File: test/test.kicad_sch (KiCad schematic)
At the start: 3 parts, among them U1 CHIP-PRO

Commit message: big update
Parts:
- LedRef: renamed from D1; value LED -> 100V; footprint LED_SMD:LED_01005_0402Metric -> (none)
- U1: value CHIP-PRO -> CHIP; now not fitted; now left out of the parts list
- renumbered R1 to REFR
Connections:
- net at U1.18 (HPL): now also U1.22 (PB6/I2S-BCLK), U1.23 (PB7/I2S-LCLK), U1.24 (PB8/I2S-DO), U1.25 (PB9/I2S-DI); no longer REFR.2
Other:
- company: SELAB INC -> (none)
- moved on the sheet: REFR
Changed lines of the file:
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@@
 		(title "BestBoard")
 		(date "2026-07-03")
-		(rev "v1")
-		(company "SELAB INC")
 		(comment 1 "c1")
+		(comment 2 "dsaf")
 	)
 	(junction
@@
 		(color 0 0 0 0)
 	)
+	(junction
+		(at 171.45 100.33)
+		(diameter 0)
+		(color 0 0 0 0)
+	)
+	(junction
+		(at 171.45 102.87)
+		(diameter 0)
+		(color 0 0 0 0)
+	)
+	(junction
+		(at 171.45 97.79)
+		(diameter 0)
+		(color 0 0 0 0)
+	)
+	(junction
+		(at 171.45 95.25)
+		(diameter 0)
+		(color 0 0 0 0)
+	)
 	(wire
 		(pts
@@
 	(wire
 		(pts
+			(xy 171.45 102.87) (xy 171.45 107.95)
+		)
+		(stroke
+			(width 0)
+			(type default)
+		)
+	)
+	(wire
+		(pts
+			(xy 171.45 100.33) (xy 171.45 102.87)
+		)
+		(stroke
+			(width 0)
+			(type default)
+		)
+	)
+	(wire
+		(pts
 			(xy 161.29 130.81) (xy 171.45 130.81)
 		)
@@
 	(wire
 		(pts
-			(xy 171.45 106.68) (xy 171.45 107.95)
+			(xy 171.45 93.98) (xy 171.45 95.25)
+		)
+		(stroke
+			(width 0)
+			(type default)
+		)
+	)
+	(wire
+		(pts
+			(xy 171.45 95.25) (xy 171.45 97.79)
 		)
 		(stroke
@@
 	(wire
 		(pts
-			(xy 76.2 106.68) (xy 171.45 106.68)
+			(xy 171.45 97.79) (xy 171.45 100.33)
+		)
+		(stroke
+			(width 0)
+			(type default)
+		)
+	)
+	(wire
+		(pts
+			(xy 24.13 93.98) (xy 171.45 93.98)
 		)
 		(stroke
@@
 		(body_style 1)
 		(exclude_from_sim no)
-		(in_bom yes)
-		(on_board yes)
+		(in_bom no)
+		(on_board no)
 		(in_pos_files yes)
-		(dnp no)
+		(dnp yes)
 		(fields_autoplaced yes)
 		(property "Reference" "U1"
@@
 			)
 		)
-		(property "Value" "CHIP-PRO"
+		(property "Value" "CHIP"
 			(at 214.2333 57.15 0)
 			(show_name no)
@@
 		(dnp no)
 		(fields_autoplaced yes)
-		(property "Reference" "D1"
+		(property "Reference" "LedRef"
 			(at 129.2225 59.69 0)
 			(show_name no)
@@
 			)
 		)
-		(property "Value" "LED"
+		(property "Value" "100V"
 			(at 129.2225 62.23 0)
 			(show_name no)
@@
 			)
 		)
-		(property "Footprint" "LED_SMD:LED_01005_0402Metric"
+		(property "Footprint" ""
 			(at 130.81 66.04 0)
 			(hide yes)
@@
 			(project "test"
 				(path "/2fe60de8-5e34-47a1-855a-3a2b581508e8"
-					(reference "D1")
+					(reference "LedRef")
 					(unit 1)
 				)
@@
 	(symbol
 		(lib_id "Device:R")
-		(at 76.2 102.87 0)
+		(at 24.13 90.17 270)
 		(unit 1)
 		(body_style 1)
@@
 		(dnp no)
 		(fields_autoplaced yes)
-		(property "Reference" "R1"
-			(at 78.74 101.5999 0)
-			(show_name no)
-			(do_not_autoplace no)
-			(effects
-				(font
-					(size 1.27 1.27)
-				)
-				(justify left)
+		(property "Reference" "REFR"
+			(at 24.13 83.82 90)
+			(show_name no)
+			(do_not_autoplace no)
+			(effects
+				(font
+					(size 1.27 1.27)
+				)
 			)
 		)
 		(property "Value" "R"
-			(at 78.74 104.1399 0)
-			(show_name no)
-			(do_not_autoplace no)
-			(effects
-				(font
-					(size 1.27 1.27)
-				)
-				(justify left)
+			(at 24.13 86.36 90)
+			(show_name no)
+			(do_not_autoplace no)
+			(effects
+				(font
+					(size 1.27 1.27)
+				)
 			)
 		)
 		(property "Footprint" "Resistor_SMD:R_01005_0402Metric"
-			(at 74.422 102.87 90)
+			(at 24.13 88.392 90)
 			(hide yes)
 			(show_name no)
@@
 		)
 		(property "Datasheet" ""
-			(at 76.2 102.87 0)
+			(at 24.13 90.17 0)
 			(hide yes)
 			(show_name no)
@@
 		)
 		(property "Description" "Resistor"
-			(at 76.2 102.87 0)
+			(at 24.13 90.17 0)
 			(hide yes)
 			(show_name no)
@@
 			(project "test"
 				(path "/2fe60de8-5e34-47a1-855a-3a2b581508e8"
-					(reference "R1")
+					(reference "REFR")
 					(unit 1)
 				)

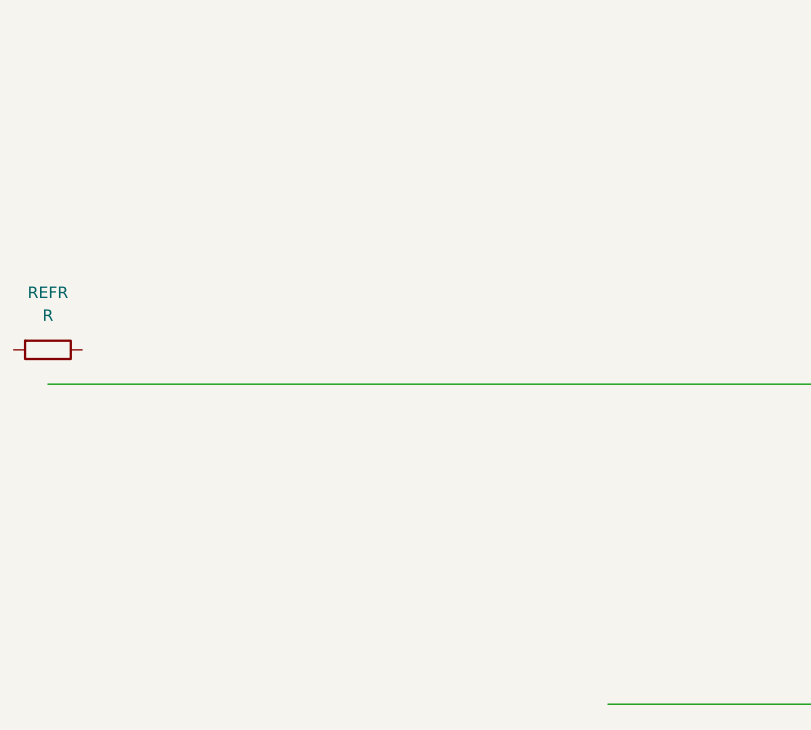
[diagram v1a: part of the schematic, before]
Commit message: added 2 subsheets
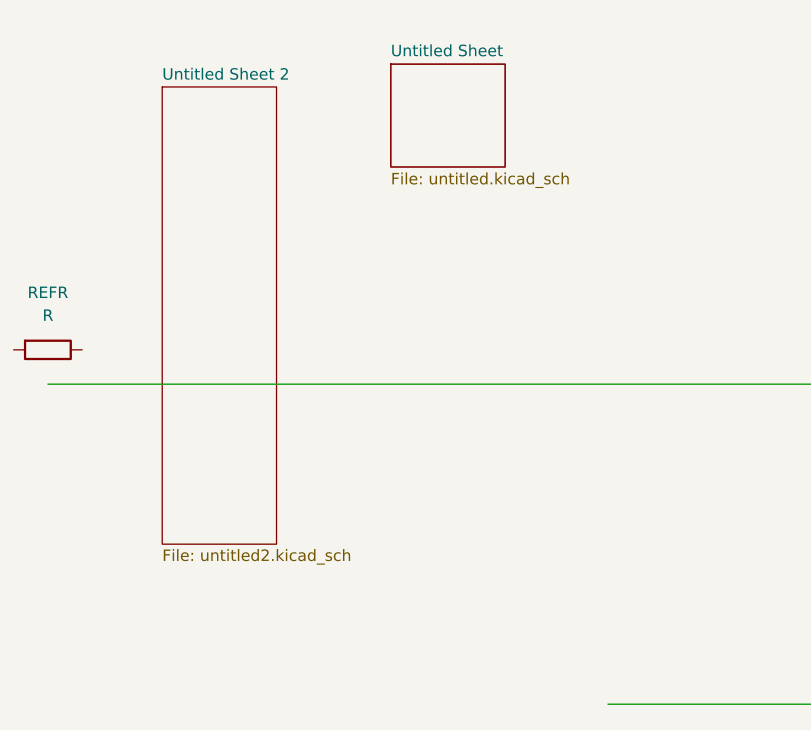
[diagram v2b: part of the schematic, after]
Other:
- added sheet Untitled Sheet (untitled.kicad_sch)
- added sheet Untitled Sheet 2 (untitled2.kicad_sch)
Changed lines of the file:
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@@
+		)
+	)
+	(sheet
+		(at 62.23 58.42)
+		(size 12.7 11.43)
+		(exclude_from_sim no)
+		(in_bom yes)
+		(on_board yes)
+		(dnp no)
+		(fields_autoplaced yes)
+		(stroke
+			(width 0.1778)
+			(type solid)
+		)
+		(fill
+			(color 0 0 0 0)
+		)
+		(property "Sheetname" "Untitled Sheet"
+			(at 62.23 57.6957 0)
+			(show_name no)
+			(do_not_autoplace no)
+			(effects
+				(font
+					(size 1.27 1.27)
+				)
+				(justify left bottom)
+			)
+		)
+		(property "Sheetfile" "untitled.kicad_sch"
+			(at 62.23 70.4473 0)
+			(show_name no)
+			(do_not_autoplace no)
+			(effects
+				(font
+					(size 1.27 1.27)
+				)
+				(justify left top)
+			)
+		)
+		(instances
+			(project "test"
+				(path "/2fe60de8-5e34-47a1-855a-3a2b581508e8"
+					(page "2")
+				)
+			)
+		)
+	)
+	(sheet
+		(at 36.83 60.96)
+		(size 12.7 50.8)
+		(exclude_from_sim no)
+		(in_bom yes)
+		(on_board yes)
+		(dnp no)
+		(fields_autoplaced yes)
+		(stroke
+			(width 0.0508)
+			(type solid)
+		)
+		(fill
+			(color 0 0 0 0)
+		)
+		(property "Sheetname" "Untitled Sheet 2"
+			(at 36.83 60.2992 0)
+			(show_name no)
+			(do_not_autoplace no)
+			(effects
+				(font
+					(size 1.27 1.27)
+				)
+				(justify left bottom)
+			)
+		)
+		(property "Sheetfile" "untitled2.kicad_sch"
+			(at 36.83 112.2938 0)
+			(show_name no)
+			(do_not_autoplace no)
+			(effects
+				(font
+					(size 1.27 1.27)
+				)
+				(justify left top)
+			)
+		)
+		(instances
+			(project "test"
+				(path "/2fe60de8-5e34-47a1-855a-3a2b581508e8"
+					(page "3")
+				)
+			)
 		)
 	)

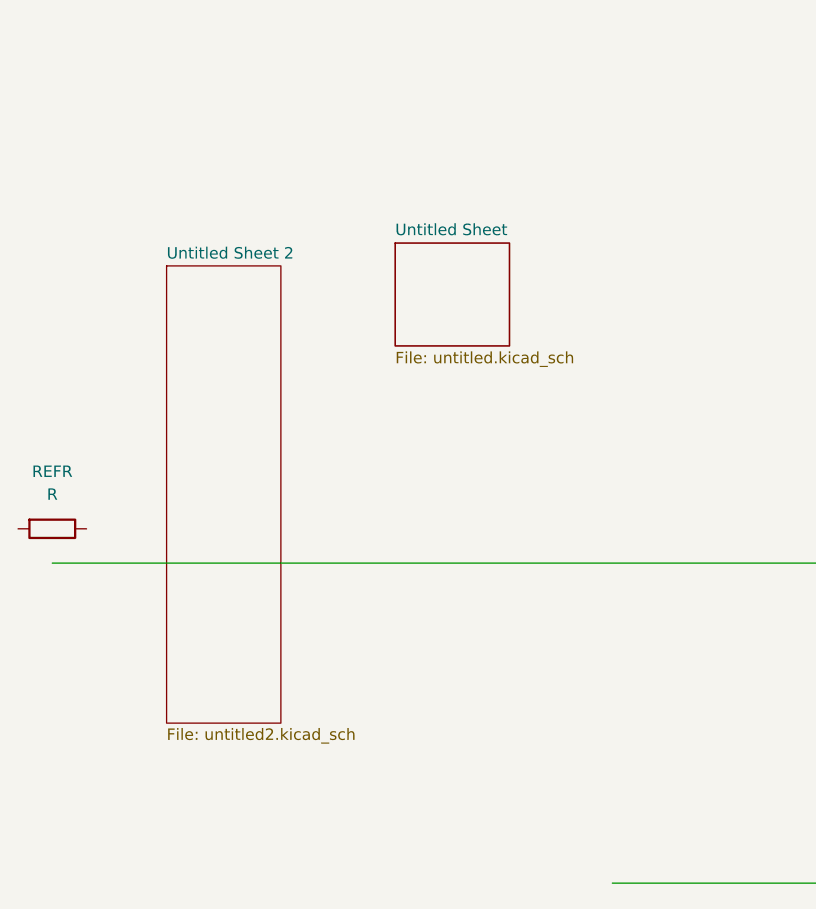
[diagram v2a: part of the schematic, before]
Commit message: changed the position of the name, the name and the file of one subsheet. moved other subsheet and rotated it
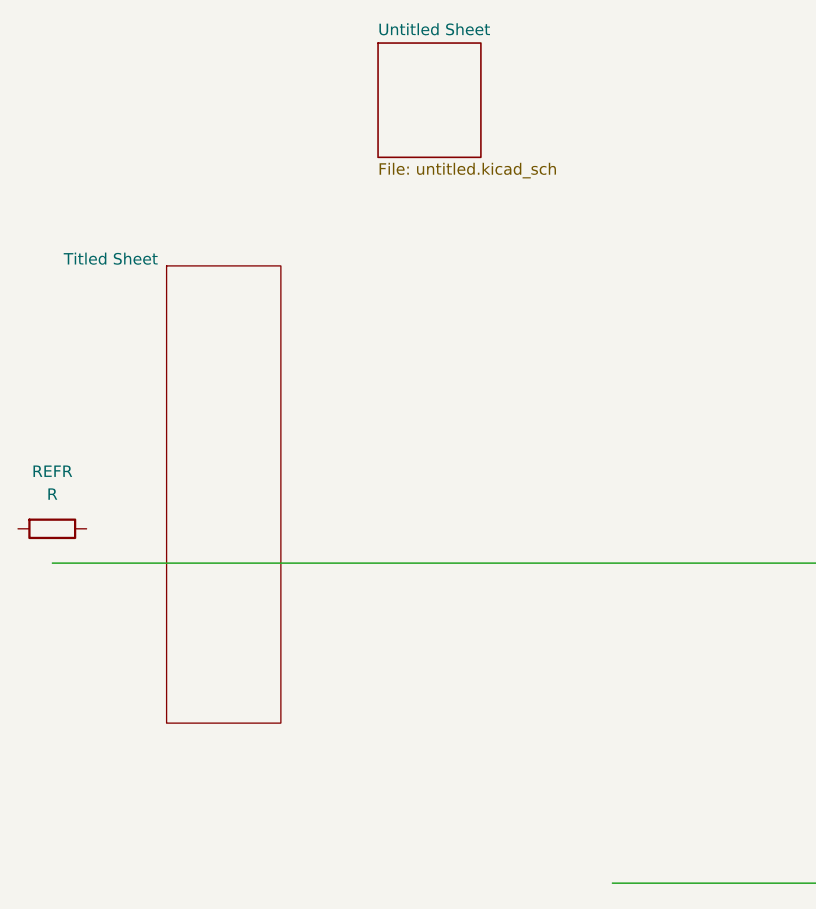
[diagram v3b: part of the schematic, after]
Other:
- sheet Untitled Sheet 2 renamed Titled Sheet
- sheet Titled Sheet: file untitled2.kicad_sch -> titled.kicad_sch
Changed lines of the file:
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@@
 	)
 	(sheet
-		(at 62.23 58.42)
-		(size 12.7 11.43)
+		(at 60.325 36.195)
+		(size 11.43 12.7)
 		(exclude_from_sim no)
 		(in_bom yes)
@@
 		)
 		(property "Sheetname" "Untitled Sheet"
-			(at 62.23 57.6957 0)
+			(at 60.325 35.4707 0)
 			(show_name no)
 			(do_not_autoplace no)
@@
 		)
 		(property "Sheetfile" "untitled.kicad_sch"
-			(at 62.23 70.4473 0)
+			(at 60.325 49.4923 0)
 			(show_name no)
 			(do_not_autoplace no)
@@
 		(on_board yes)
 		(dnp no)
-		(fields_autoplaced yes)
 		(stroke
 			(width 0.0508)
@@
 			(color 0 0 0 0)
 		)
-		(property "Sheetname" "Untitled Sheet 2"
-			(at 36.83 60.2992 0)
+		(property "Sheetname" "Titled Sheet"
+			(at 25.4 60.96 0)
 			(show_name no)
 			(do_not_autoplace no)
@@
 			)
 		)
-		(property "Sheetfile" "untitled2.kicad_sch"
+		(property "Sheetfile" "titled.kicad_sch"
 			(at 36.83 112.2938 0)
+			(hide yes)
 			(show_name no)
 			(do_not_autoplace no)
